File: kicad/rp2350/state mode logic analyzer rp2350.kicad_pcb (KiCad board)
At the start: 4 copper layers, 82.8 x 56.7 mm, 134 parts, among them J1 USB0, J2 5V USB0, J3 Exp Out, J4 Exp In, J5 Probe, J6 Probe Power, J7 SWD0, SW1 Reset 0, SW2 Boot 0, U1 RP2040, U10 74LVC245APW, U11 74LVC245APW, U3 74HC4520D, U4 LTC6994xS6-1, U5 MCP4725, U6 AD5241BRZ1M, U7 IS25LP128F-JBLE, U9 MCP1826S, Y1 ECS-120-18-33-JEM-TR

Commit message: end of stream commit
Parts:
- removed C10, C12: 10u, Capacitor_SMD:C_0805_2012Metric
- removed C11, C7, C8, C9: 1u, Capacitor_SMD:C_0603_1608Metric_Pad1.08x0.95mm_HandSolder
- removed D6: 2040_L0, LED_SMD:LED_1206_3216Metric_Pad1.42x1.75mm_HandSolder
- removed J3: Exp Out, Connector_PinHeader_2.54mm:PinHeader_2x10_P2.54mm_Horizontal
- removed J4: Exp In, Connector_PinSocket_2.54mm:PinSocket_2x10_P2.54mm_Horizontal
- removed R1, R2: 4k7, Resistor_SMD:R_0603_1608Metric_Pad0.98x0.95mm_HandSolder
- removed R14: 1k, Resistor_SMD:R_0603_1608Metric_Pad0.98x0.95mm_HandSolder
- removed TP133, TP8, TP9: TestPoint_Harwin, My Libraries:Harwin-S1751-46-Test-Point
- removed U1: RP2040, Package_DFN_QFN:QFN-56-1EP_7x7mm_P0.4mm_EP3.2x3.2mm
- added C13: 100n, Capacitor_SMD:C_0402_1005Metric, F.Cu at (43.3, 49.9)
- added C14: 4.7u, Capacitor_SMD:C_0402_1005Metric, F.Cu at (43.3, 51.9)
- added C15: 100n, Capacitor_SMD:C_0402_1005Metric, F.Cu at (43.3, 53.8)
- added C16: 100n, Capacitor_SMD:C_0402_1005Metric, F.Cu at (43.3, 55.8)
- added C17: 100n, Capacitor_SMD:C_0402_1005Metric, F.Cu at (43.3, 57.8)
- added C18: 100n, Capacitor_SMD:C_0402_1005Metric, F.Cu at (46.2, 49.9)
- added C25: 100n, Capacitor_SMD:C_0402_1005Metric, F.Cu at (46.2, 51.9)
- added C26: 100n, Capacitor_SMD:C_0402_1005Metric, F.Cu at (46.2, 53.8)
- added C27: 100n, Capacitor_SMD:C_0402_1005Metric, F.Cu at (46.2, 55.8)
- added C28: 100n, Capacitor_SMD:C_0402_1005Metric, F.Cu at (46.2, 57.8)
- added C29: 100n, Capacitor_SMD:C_0402_1005Metric, F.Cu at (49.1, 49.9)
- added C30: 100n, Capacitor_SMD:C_0402_1005Metric, F.Cu at (49.1, 51.9)
- added C32: 4.7u, RP2350_80QFN_minimal:C_0402_1005Metric_small_pads, F.Cu at (53.5, 32.5)
- added C33: 4.7u, RP2350_80QFN_minimal:C_0402_1005Metric_small_pads, F.Cu at (53.5, 34.5)
- added C34: 4.7u, Capacitor_SMD:C_0402_1005Metric, F.Cu at (49.1, 53.8)
- added D8: 2040_L0, LED_SMD:LED_1206_3216Metric_Pad1.42x1.75mm_HandSolder, F.Cu at (53.5, 56.4)
- added H4: MountingHole, MountingHole:MountingHole_2.7mm, F.Cu at (45.4, 62.2)
- added L1: 3.3u, RP2350_80QFN_minimal:L_pol_2016, F.Cu at (53.8, 37.5)
- added R41: 4k7, Resistor_SMD:R_0603_1608Metric_Pad0.98x0.95mm_HandSolder, F.Cu at (51.0, 60.0)
- added R42: 4k7, Resistor_SMD:R_0603_1608Metric_Pad0.98x0.95mm_HandSolder, F.Cu at (51.0, 62.5)
- added R43: 1k, Resistor_SMD:R_0603_1608Metric_Pad0.98x0.95mm_HandSolder, F.Cu at (51.0, 65.0)
- added R44: 33, Resistor_SMD:R_0402_1005Metric, F.Cu at (54.6, 59.7)
- added TP21: TestPoint_Harwin, My Libraries:Harwin-S1751-46-Test-Point, F.Cu at (52.7, 50.3)
- added TP22: TestPoint_Harwin, My Libraries:Harwin-S1751-46-Test-Point, F.Cu at (52.7, 53.2)
- added U2: RP2350_80QFN, RP2350_80QFN_minimal:RP2350-QFN-80-1EP_10x10_P0.4mm_EP3.4x3.4mm_ThermalVias, F.Cu at (82.2, 59.4)
- U6: footprint Package_SO:SOIC-14_3.9x8.7mm_P1.27mm -> Package_SO:SOIC-16_3.9x9.9mm_P1.27mm
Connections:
- net /XIN renamed Net-(U2-XIN)
- R12 pad 1: /XOUT -> Net-(U2-XOUT)
- U9 pad 4: GND -> (no net)
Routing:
- net /CNT_RESET: track 136.9 -> 0.00 mm, vias 5 -> 0
- net /LA_Enable: track 132.3 -> 0.00 mm, vias 1 -> 0
- net +3V3: track 117.3 -> 0.00 mm, vias 35 -> 0
- net /CLK: track 115.9 -> 0.00 mm, vias 2 -> 0
- net /SDA: track 97.8 -> 0.00 mm, vias 2 -> 0
- net /CNT_CLK: track 97.4 -> 0.00 mm, vias 4 -> 0
- net /SCL: track 91.5 -> 0.00 mm, vias 2 -> 0
- net /TS0: track 88.2 -> 0.00 mm, vias 1 -> 0
- net /Run: track 82.6 -> 0.00 mm, vias 2 -> 0
- net /TS1: track 82.4 -> 0.00 mm, vias 1 -> 0
- net /TS3: track 82.4 -> 0.00 mm, vias 1 -> 0
- net /TS2: track 81.7 -> 0.00 mm, vias 1 -> 0
- net +5V: track 81.3 -> 0.00 mm, vias 1 -> 0
- net GND: track 79.7 -> 0.00 mm, vias 62 -> 0
- net /TS4: track 73.9 -> 0.00 mm, vias 1 -> 0
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
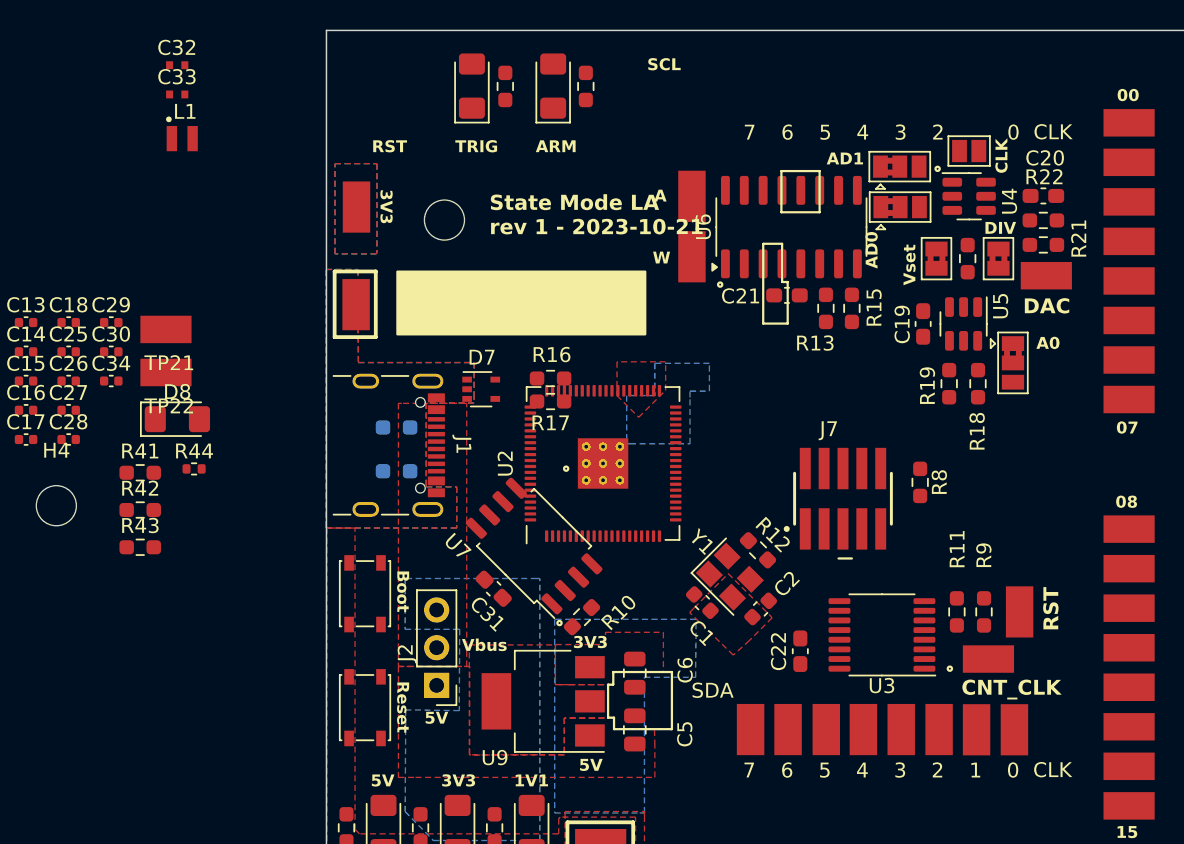
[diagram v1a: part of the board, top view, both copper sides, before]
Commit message: removed clock delay and timestamp counter since it can be done in pio.
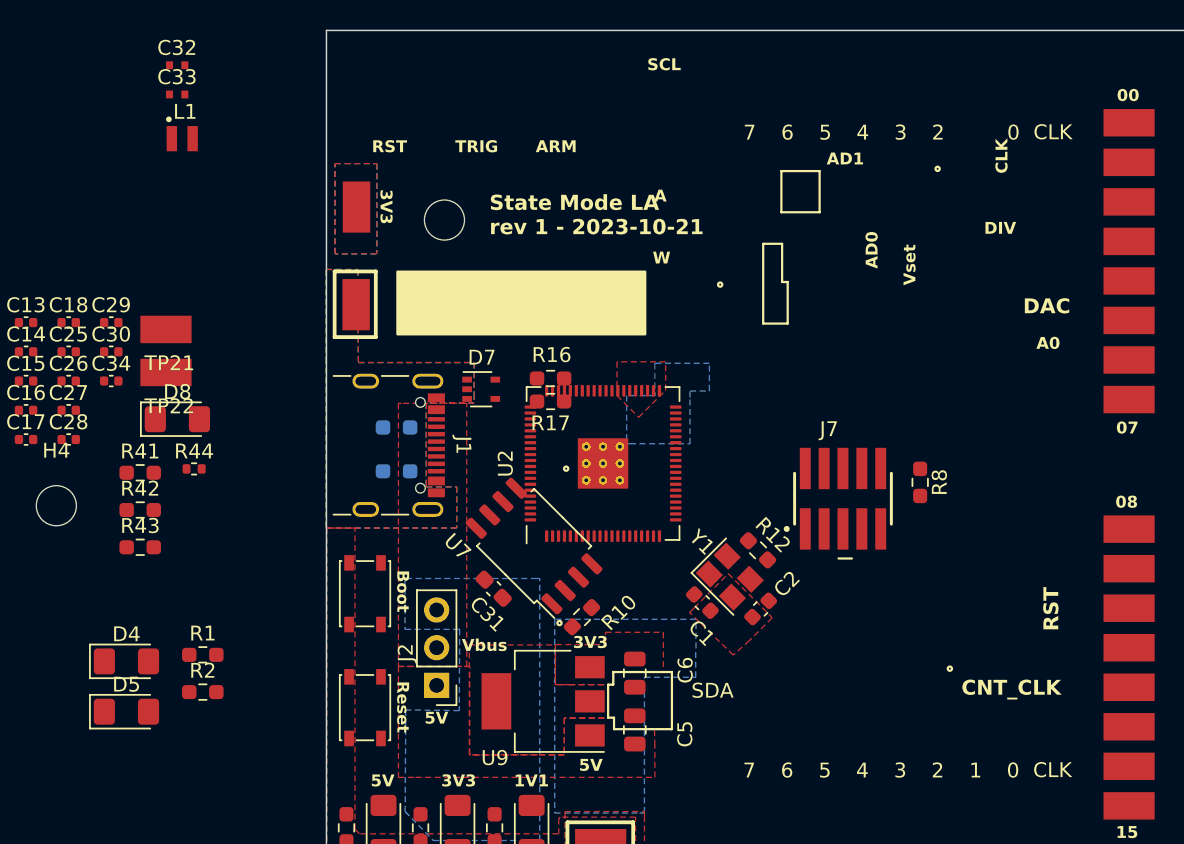
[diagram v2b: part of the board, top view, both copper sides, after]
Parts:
- removed C19, C20, C21, C22: 1u, Capacitor_SMD:C_0603_1608Metric_Pad1.08x0.95mm_HandSolder
- removed JP1: AD0, Jumper:SolderJumper-3_P1.3mm_Bridged2Bar12_Pad1.0x1.5mm
- removed JP2: AD1, Jumper:SolderJumper-3_P1.3mm_Bridged2Bar12_Pad1.0x1.5mm
- removed JP3: A0, Jumper:SolderJumper-3_P1.3mm_Bridged2Bar12_Pad1.0x1.5mm
- removed JP4, JP5: DAC Disable, Jumper:SolderJumper-2_P1.3mm_Bridged2Bar_Pad1.0x1.5mm
- removed JP6: CLK Bypass, Jumper:SolderJumper-2_P1.3mm_Open_Pad1.0x1.5mm
- removed R11, R13, R15, R18, R19, R9: 0, Resistor_SMD:R_0603_1608Metric_Pad0.98x0.95mm_HandSolder
- removed R20, R21, R22: DNP, Resistor_SMD:R_0603_1608Metric_Pad0.98x0.95mm_HandSolder
- removed R3, R4: 1k, Resistor_SMD:R_0603_1608Metric_Pad0.98x0.95mm_HandSolder
- removed TP0, TP1, TP10, TP11, TP12, TP13, TP14, TP2, TP3, TP4, TP5, TP6, TP7: TestPoint_Harwin, My Libraries:Harwin-S1751-46-Test-Point
- removed U3: 74HC4520D, Package_SO:TSSOP-16_4.4x5mm_P0.65mm
- removed U4: LTC6994xS6-1, Package_TO_SOT_SMD:TSOT-23-6
- removed U5: MCP4725, Package_TO_SOT_SMD:SOT-23-6
- removed U6: AD5241BRZ1M, Package_SO:SOIC-16_3.9x9.9mm_P1.27mm
- added R1: 1k, Resistor_SMD:R_0603_1608Metric_Pad0.98x0.95mm_HandSolder, F.Cu at (55.2, 72.3)
- added R2: 1k, Resistor_SMD:R_0603_1608Metric_Pad0.98x0.95mm_HandSolder, F.Cu at (55.2, 74.8)
- moved D4 48.3 mm to (50.1, 72.7), turned to 0 degrees
- moved D5 48.1 mm to (50.1, 76.1), turned to 0 degrees
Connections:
- U2 pad 48: /CLK -> unconnected-(U2-GPIO39-Pad48)
- U2 pad 49: /TS0 -> unconnected-(U2-GPIO40_ADC0-Pad49)
- U2 pad 52: /TS1 -> unconnected-(U2-GPIO41_ADC1-Pad52)
- U2 pad 53: /TS2 -> unconnected-(U2-GPIO42_ADC2-Pad53)
- U2 pad 54: /TS3 -> unconnected-(U2-GPIO43_ADC3-Pad54)
- U2 pad 55: /TS4 -> unconnected-(U2-GPIO44_ADC4-Pad55)
- U2 pad 56: /TS5 -> unconnected-(U2-GPIO45_ADC5-Pad56)
- U2 pad 57: /TS6 -> Net-(U2-GPIO46_ADC6)
- U2 pad 58: /TS7 -> Net-(U2-GPIO47_ADC7)

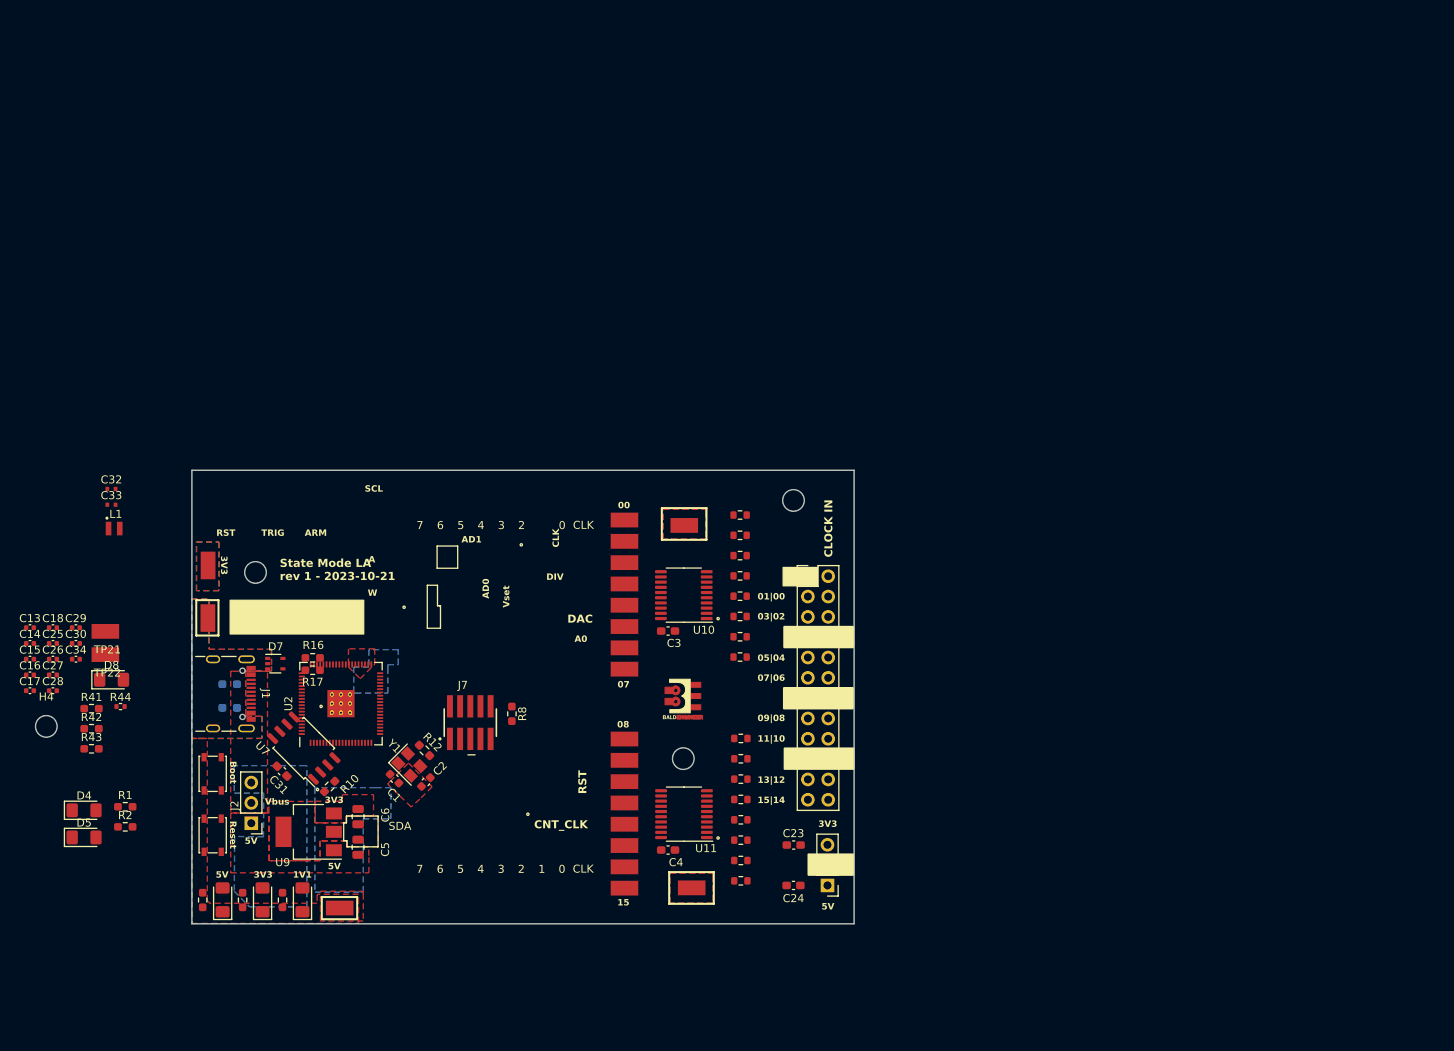
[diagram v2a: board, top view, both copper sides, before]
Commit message: moved to 2-supply buffer design
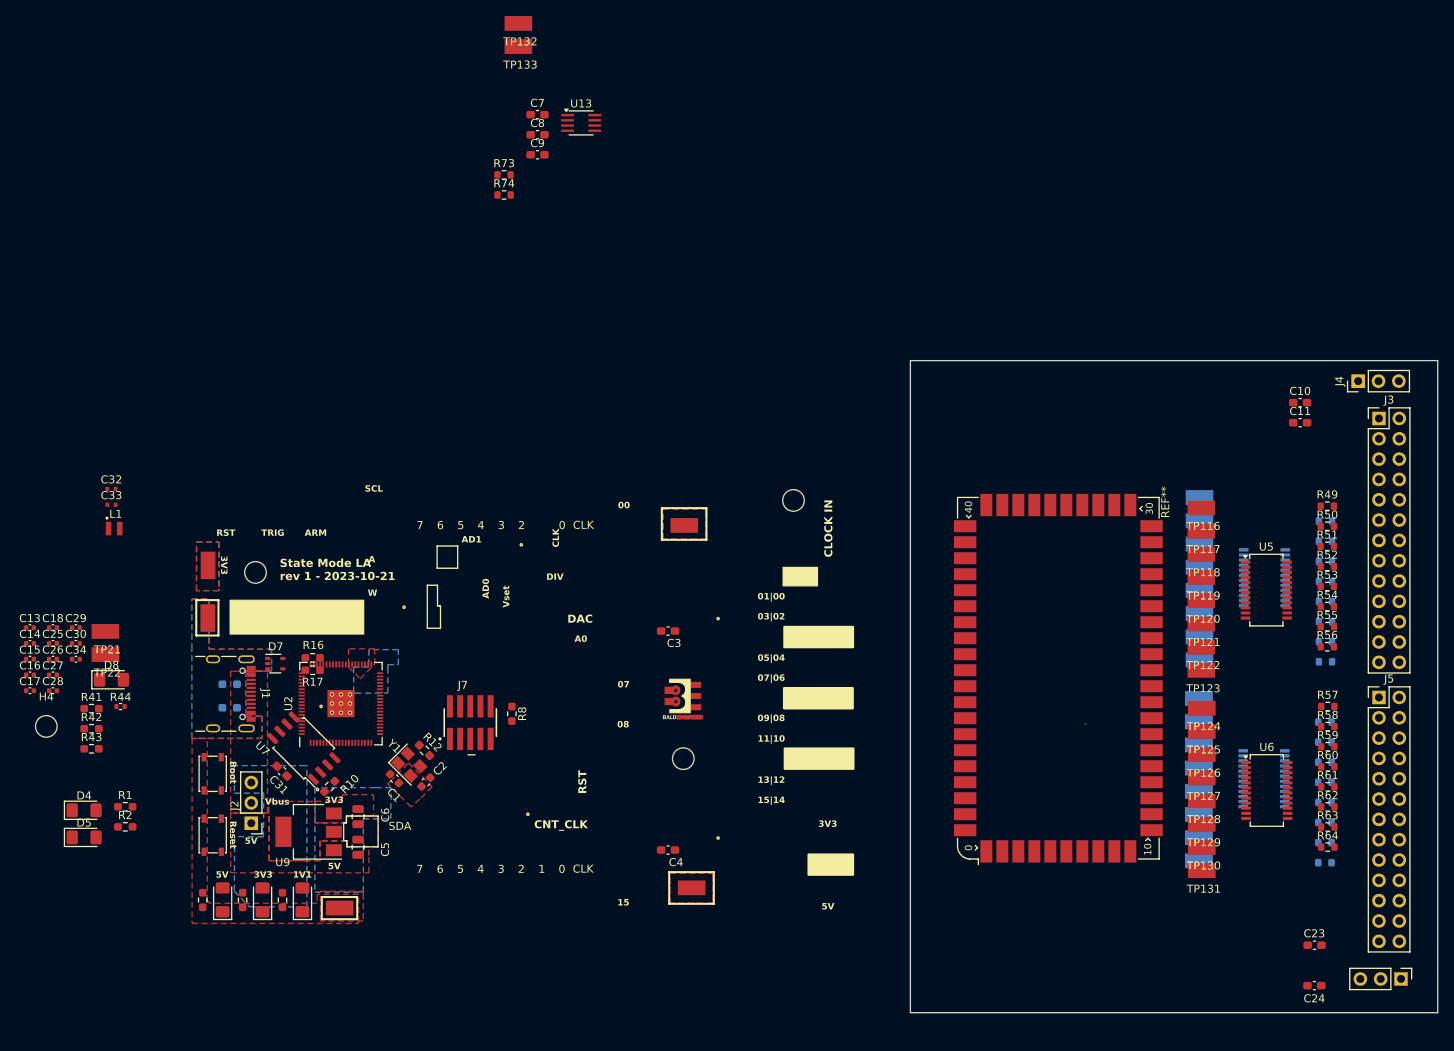
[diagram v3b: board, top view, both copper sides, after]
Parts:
- removed U10, U11: 74LVC245APW, Package_SO:TSSOP-20_4.4x6.5mm_P0.65mm
- added C10: 1u, Capacitor_SMD:C_0603_1608Metric_Pad1.08x0.95mm_HandSolder, F.Cu at (202.1, 21.8)
- added C11: 1u, Capacitor_SMD:C_0603_1608Metric_Pad1.08x0.95mm_HandSolder, F.Cu at (202.1, 24.3)
- added C7: 1u, Capacitor_SMD:C_0603_1608Metric_Pad1.08x0.95mm_HandSolder, F.Cu at (106.8, -14.2)
- added C8: 1u, Capacitor_SMD:C_0603_1608Metric_Pad1.08x0.95mm_HandSolder, F.Cu at (106.8, -11.7)
- added C9: 1u, Capacitor_SMD:C_0603_1608Metric_Pad1.08x0.95mm_HandSolder, F.Cu at (106.8, -9.23)
- added J3: Probe_Hi, Connector_PinHeader_2.54mm:PinHeader_2x13_P2.54mm_Vertical, F.Cu at (211.9, 23.7)
- added J4: Probe Power, Connector_PinHeader_2.54mm:PinHeader_1x03_P2.54mm_Vertical, F.Cu at (209.3, 19.1)
- added R49: 220, Resistor_SMD:R_0603_1608Metric, F.Cu at (205.5, 34.7)
- added R50: 220, Resistor_SMD:R_0603_1608Metric, F.Cu at (205.5, 37.2)
- added R51: 220, Resistor_SMD:R_0603_1608Metric, F.Cu at (205.5, 39.7)
- added R52: 220, Resistor_SMD:R_0603_1608Metric, F.Cu at (205.5, 42.2)
- added R53: 220, Resistor_SMD:R_0603_1608Metric, F.Cu at (205.5, 44.7)
- added R54: 220, Resistor_SMD:R_0603_1608Metric, F.Cu at (205.5, 47.2)
- added R55: 220, Resistor_SMD:R_0603_1608Metric, F.Cu at (205.5, 49.8)
- added R56: 220, Resistor_SMD:R_0603_1608Metric, F.Cu at (205.5, 52.3)
- added R57: 220, Resistor_SMD:R_0603_1608Metric, F.Cu at (205.5, 59.7)
- added R58: 220, Resistor_SMD:R_0603_1608Metric, F.Cu at (205.5, 62.2)
- added R59: 220, Resistor_SMD:R_0603_1608Metric, F.Cu at (205.5, 64.8)
- added R60: 220, Resistor_SMD:R_0603_1608Metric, F.Cu at (205.5, 67.3)
- added R61: 220, Resistor_SMD:R_0603_1608Metric, F.Cu at (205.5, 69.8)
- added R62: 220, Resistor_SMD:R_0603_1608Metric, F.Cu at (205.5, 72.3)
- added R63: 220, Resistor_SMD:R_0603_1608Metric, F.Cu at (205.5, 74.8)
- added R64: 220, Resistor_SMD:R_0603_1608Metric, F.Cu at (205.5, 77.3)
- added R73: 220, Resistor_SMD:R_0603_1608Metric, F.Cu at (102.6, -6.72)
- added R74: 220, Resistor_SMD:R_0603_1608Metric, F.Cu at (102.6, -4.21)
- added REF**: RP2xxx_Stamp_XL_SMD, KiCad:RP2xxx_Stamp_XL_SMD, F.Cu at (171.9, 56.2)
- added TP116: TestPoint_Harwin, My Libraries:Harwin-S1751-46-Test-Point, F.Cu at (189.7, 34.9)
- added TP117: TestPoint_Harwin, My Libraries:Harwin-S1751-46-Test-Point, F.Cu at (189.7, 37.8)
- added TP118: TestPoint_Harwin, My Libraries:Harwin-S1751-46-Test-Point, F.Cu at (189.7, 40.7)
- added TP119: TestPoint_Harwin, My Libraries:Harwin-S1751-46-Test-Point, F.Cu at (189.7, 43.6)
- added TP120: TestPoint_Harwin, My Libraries:Harwin-S1751-46-Test-Point, F.Cu at (189.7, 46.5)
- added TP121: TestPoint_Harwin, My Libraries:Harwin-S1751-46-Test-Point, F.Cu at (189.7, 49.4)
- added TP122: TestPoint_Harwin, My Libraries:Harwin-S1751-46-Test-Point, F.Cu at (189.7, 52.3)
- added TP123: TestPoint_Harwin, My Libraries:Harwin-S1751-46-Test-Point, F.Cu at (189.7, 55.2)
- added TP124: TestPoint_Harwin, My Libraries:Harwin-S1751-46-Test-Point, F.Cu at (189.8, 60.0)
- added TP125: TestPoint_Harwin, My Libraries:Harwin-S1751-46-Test-Point, F.Cu at (189.8, 62.9)
- added TP126: TestPoint_Harwin, My Libraries:Harwin-S1751-46-Test-Point, F.Cu at (189.8, 65.8)
- added TP127: TestPoint_Harwin, My Libraries:Harwin-S1751-46-Test-Point, F.Cu at (189.8, 68.7)
- added TP128: TestPoint_Harwin, My Libraries:Harwin-S1751-46-Test-Point, F.Cu at (189.8, 71.6)
- added TP129: TestPoint_Harwin, My Libraries:Harwin-S1751-46-Test-Point, F.Cu at (189.8, 74.5)
- added TP130: TestPoint_Harwin, My Libraries:Harwin-S1751-46-Test-Point, F.Cu at (189.8, 77.4)
- added TP131: TestPoint_Harwin, My Libraries:Harwin-S1751-46-Test-Point, F.Cu at (189.8, 80.3)
- added TP132: TestPoint_Harwin, My Libraries:Harwin-S1751-46-Test-Point, F.Cu at (104.4, -25.7)
- added TP133: TestPoint_Harwin, My Libraries:Harwin-S1751-46-Test-Point, F.Cu at (104.4, -22.8)
- added U12: SN74LVC8T245, Package_SO:SSOP-24_3.9x8.7mm_P0.635mm, B.Cu at (197.6, 68.8)
- added U13: SN74LVC2T45DCUR, Package_SO:SSOP-8_2.95x2.8mm_P0.65mm, F.Cu at (112.2, -13.2)
- added U4: SN74LVC8T245, Package_SO:SSOP-24_3.9x8.7mm_P0.635mm, B.Cu at (197.6, 43.6)
- added U5: SN74LVC8T245, Package_SO:SSOP-24_3.9x8.7mm_P0.635mm, F.Cu at (197.9, 45.2)
- added U6: SN74LVC8T245, Package_SO:SSOP-24_3.9x8.7mm_P0.635mm, F.Cu at (197.9, 70.2)
- J5: value Probe -> Probe_Lo; footprint Connector_PinHeader_2.54mm:PinHeader_2x12_P2.54mm_Vertical -> Connector_PinHeader_2.54mm:PinHeader_2x13_P2.54mm_Vertical
- R25, R26, R27, R28, R29, R30, R31, R32, R33, R34, R35, R36, R37, R38, R39, R40, TP100, TP101, TP102, TP103, TP104, TP105, TP106, TP107, TP108, TP109, TP110, TP111, TP112, TP113, TP114, TP115: moved to B.Cu
- moved TP115 86.9 mm to (189.5, 33.6)
- moved R40 85.8 mm to (205.2, 36.6), turned to 0 degrees
- moved R25 85.0 mm to (205.2, 79.3)
- moved TP114 83.9 mm to (189.5, 36.5)
- moved TP100 83.5 mm to (189.4, 79.0)
- moved R39 83.3 mm to (205.2, 39.1), turned to 0 degrees
- moved R26 82.6 mm to (205.2, 76.7)
- moved TP113 81.2 mm to (189.5, 39.4)
- moved R38 81.0 mm to (205.2, 41.6), turned to 0 degrees
- moved TP101 80.8 mm to (189.4, 76.1)
- moved R27 80.4 mm to (205.2, 74.2)
- moved R37 78.9 mm to (205.2, 44.1), turned to 0 degrees
- moved TP112 78.7 mm to (189.5, 42.3)
- moved TP102 78.4 mm to (189.4, 73.2)
- moved R28 78.4 mm to (205.2, 71.7)
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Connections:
- J5 pad 1: GND -> /INQUAL
- J5 pad 10: /IN04 -> GND
- J5 pad 11: /IN07 -> /IN05
- J5 pad 12: /IN06 -> /IN04
- J5 pad 13: GND -> /IN07
- J5 pad 14: GND -> /IN06
- J5 pad 15: /IN09 -> GND
- J5 pad 16: /IN08 -> GND
- J5 pad 17: /IN11 -> /IN09
- J5 pad 18: /IN10 -> /IN08
- J5 pad 19: GND -> /IN11
- J5 pad 2: /IN_CLK -> /INCLK
- J5 pad 20: GND -> /IN10
- J5 pad 21: /IN13 -> GND
- J5 pad 22: /IN12 -> GND
- J5 pad 23: /IN15 -> /IN13
- J5 pad 24: /IN14 -> /IN12
- J5 pad 3: /IN01 -> GND
- J5 pad 4: /IN00 -> GND
- J5 pad 5: /IN03 -> /IN01
- J5 pad 6: /IN02 -> /IN00
- J5 pad 7: GND -> /IN03
- J5 pad 8: GND -> /IN02
- J5 pad 9: /IN05 -> GND
- R25 pad 1: /IN00 -> /B0
- R25 pad 2: /A0 -> /IN00
- R26 pad 1: /IN01 -> /B1
- R26 pad 2: /A1 -> /IN01
- R27 pad 1: /IN02 -> /B2
- R27 pad 2: /A2 -> /IN02
- R28 pad 1: /IN03 -> /B3
- R28 pad 2: /A3 -> /IN03
- R29 pad 1: /IN04 -> /B4
- R29 pad 2: /A4 -> /IN04
- R30 pad 1: /IN05 -> /B5
- R30 pad 2: /A5 -> /IN05
- R31 pad 1: /IN06 -> /B6
- R31 pad 2: /A6 -> /IN06
- R32 pad 1: /IN07 -> /B7
- R32 pad 2: /A7 -> /IN07
- R33 pad 1: /IN08 -> /B15
- R33 pad 2: /A8 -> /IN15
- R34 pad 1: /IN09 -> /B14
- R34 pad 2: /A9 -> /IN14
- R35 pad 1: /IN10 -> /B13
- R35 pad 2: /A10 -> /IN13
- R36 pad 1: /IN11 -> /B12
- R36 pad 2: /A11 -> /IN12
- R37 pad 1: /IN12 -> /B11
- R37 pad 2: /A12 -> /IN11
- R38 pad 1: /IN13 -> /B10
- R38 pad 2: /A13 -> /IN10
- R39 pad 1: /IN14 -> /B9
- R39 pad 2: /A14 -> /IN09
- R40 pad 1: /IN15 -> /B8
- R40 pad 2: /A15 -> /IN08
- U2 pad 1: /LA_Enable -> /BUF29
- U2 pad 11: /BUF25 -> /BUF21
- U2 pad 12: /BUF24 -> /BUF20
- U2 pad 13: /BUF23 -> /BUF19
- U2 pad 14: /BUF22 -> /BUF18
- U2 pad 16: /BUF21 -> /BUF17
- U2 pad 17: /BUF20 -> /BUF16
- U2 pad 18: /BUF19 -> /QUAL
- U2 pad 19: /BUF18 -> /CLK
- U2 pad 2: /CLK -> /BUF28
- U2 pad 20: /BUF17 -> /BUF15
- U2 pad 21: /BUF16 -> /BUF14
- U2 pad 22: /CLK -> /BUF13
- U2 pad 23: /BUF15 -> /BUF12
- U2 pad 25: /BUF14 -> /BUF11
- U2 pad 26: /BUF13 -> /BUF10
- U2 pad 27: /BUF12 -> /BUF09
- U2 pad 28: /BUF11 -> /BUF08
- U2 pad 3: /BUF31 -> /BUF27
- U2 pad 36: /BUF10 -> /BUF07
- U2 pad 37: /BUF09 -> /BUF06
- U2 pad 38: /BUF08 -> /BUF05
- U2 pad 39: /BUF07 -> /BUF04
- U2 pad 4: /BUF30 -> /BUF26
- U2 pad 40: /BUF06 -> /BUF03
- U2 pad 42: /BUF05 -> /BUF02
- U2 pad 43: /BUF04 -> /BUF01
- U2 pad 44: /BUF03 -> /BUF00
- U2 pad 45: /BUF02 -> unconnected-(U2-GPIO36-Pad45)
- U2 pad 46: /BUF01 -> unconnected-(U2-GPIO37-Pad46)
- U2 pad 47: /BUF00 -> unconnected-(U2-GPIO38-Pad47)
- U2 pad 52: unconnected-(U2-GPIO41_ADC1-Pad52) -> /SDA
- U2 pad 53: unconnected-(U2-GPIO42_ADC2-Pad53) -> /SCL
- U2 pad 54: unconnected-(U2-GPIO43_ADC3-Pad54) -> /CNT_CLK
- U2 pad 55: unconnected-(U2-GPIO44_ADC4-Pad55) -> /CNT_RESET
- U2 pad 56: unconnected-(U2-GPIO45_ADC5-Pad56) -> /LA_Enable
- U2 pad 6: /BUF29 -> /BUF25
- U2 pad 7: /BUF28 -> /BUF24
- U2 pad 77: /SDA -> /QUAL
- U2 pad 78: /SCL -> /CLK
- U2 pad 79: /CNT_CLK -> /BUF31
- U2 pad 8: /BUF27 -> /BUF23
- U2 pad 80: /CNT_RESET -> /BUF30
- U2 pad 9: /BUF26 -> /BUF22
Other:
- board size 82.8 x 56.7 mm -> 65.9 x 81.5 mm
